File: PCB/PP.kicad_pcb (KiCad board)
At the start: 2 copper layers, 96.5 x 58.4 mm, 39 parts, among them Q1 Q_PMOS_DGS, Q2 Q_NMOS_DGS, Q3 Q_PMOS_DGS, Q4 Q_NMOS_DGS, U1 ESP32_DEVKITV1

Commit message: Update pouleporte releaseV2
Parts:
- removed 5V_batt1, AT1, AT2, CT1, CT2, GNDT1, GNDT2, GND_BAT1, backup_out1, backup_out2, capteurNCbas1, capteurNChaut1, capteur_NC3.3Vbas1, capteur_NC3.3Vhaut1, remote_AT1, remote_AT2, remote_CT1, remote_CT2, remote_gnd1, remote_gnd2: Conn_01x01, Connector_Pin:Pin_D1.2mm_L11.3mm_W3.0mm_Flat
- removed R3: 33, Resistor_SMD:R_0603_1608Metric
- removed R4: 10k, Resistor_SMD:R_0603_1608Metric
- removed R5, R6, R7: 12, Resistor_SMD:R_0603_1608Metric_Pad1.05x0.95mm_HandSolder
- removed capteurbas1, capteurhaut1: TCRT5000, wemos:TCRT5000
- added C1: 0.01uF, Capacitor_SMD:C_0603_1608Metric, F.Cu at (126.0, 77.0)
- added C2: 2.2uf, Capacitor_SMD:C_0603_1608Metric, F.Cu at (140.4, 63.6)
- added C3: 4.7uF, Capacitor_SMD:C_0603_1608Metric, F.Cu at (134.3, 70.3)
- added C4: 1uF, Capacitor_SMD:C_0603_1608Metric, F.Cu at (140.4, 61.1)
- added IN1: Conn_01x01, Connector_Pin:Pin_D1.2mm_L11.3mm_W3.0mm_Flat, F.Cu at (145.0, 76.0)
- added IN2: Conn_01x01, Connector_Pin:Pin_D1.2mm_L11.3mm_W3.0mm_Flat, F.Cu at (145.0, 81.2)
- added J1: USB_B_Micro, Connector_USB:USB_Micro-B_Wuerth_629105150521, F.Cu at (129.0, 47.8)
- added RESET1: SW_Push_Open, Library:interrupteur, F.Cu at (109.8, 77.8)
- added SWIO1: SW_Push_Open, Library:interrupteur, F.Cu at (96.8, 77.8)
- added U2: DRV8833PWP, Package_SO:HTSSOP-16-1EP_4.4x5mm_P0.65mm_EP3.4x5mm_Mask2.46x2.31mm_ThermalVias, F.Cu at (138.6, 56.5)
- added U3: AP7361C-33E, Package_TO_SOT_SMD:SOT-223-3_TabPin2, F.Cu at (128.5, 64.9)
- Q1, Q3: value Q_PMOS_DGS -> AO4425; footprint Package_TO_SOT_SMD:SOT-23 -> Package_SO_AKL:SO-8_3.9x4.9mm_P1.27mm
- Q2, Q4: value Q_NMOS_DGS -> AO3406; footprint Package_TO_SOT_SMD:SOT-23 -> Package_TO_SOT_SMD_AKL:SOT-23
- R1: value 33 -> 10k; footprint Resistor_SMD:R_0603_1608Metric -> Capacitor_SMD:C_0603_1608Metric
- R2: footprint Resistor_SMD:R_0603_1608Metric -> Capacitor_SMD:C_0603_1608Metric
- U1: value ESP32_DEVKITV1 -> ESP32-WROOM-32; footprint wemos:devkt1_online -> RF_Module:ESP32-WROOM-32
- moved capteurlux1 106.9 mm to (147.0, 51.0)
- moved U1 56.0 mm to (108.9, 65.5)
- moved Q3 55.8 mm to (137.2, 76.2)
- moved 3V3_lux1 55.4 mm to (147.0, 55.0)
- moved GNDlux1 54.1 mm to (147.0, 46.0)
- moved R1 49.3 mm to (109.0, 80.0), turned to 90 degrees
- moved R2 49.2 mm to (107.0, 80.0), turned to 90 degrees
- moved Q2 42.9 mm to (142.2, 68.6)
- moved Q1 40.0 mm to (127.9, 72.4)
- moved MOT2 38.2 mm to (147.0, 63.0), turned to 0 degrees
- moved MOT1 38.2 mm to (147.0, 68.0), turned to 0 degrees
- moved Q4 34.4 mm to (121.6, 78.9)
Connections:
- Q1 pad 1: Net-(MOT1-Pad1) -> 5V
- Q1 pad 2: Net-(Q1-Pad2) -> 5V
- Q2 pad 1: Net-(MOT1-Pad1) -> Net-(backup_out1-Pad1)
- Q2 pad 2: Net-(Q1-Pad2) -> GND
- Q2 pad 3: GND -> Net-(MOT1-Pad1)
- Q3 pad 1: Net-(Q3-Pad1) -> 5V
- Q3 pad 2: Net-(Q3-Pad2) -> unconnected-(Q3-Pad2)
- Q3 pad 3: 5V -> unconnected-(Q3-Pad3)
- Q4 pad 1: Net-(Q3-Pad1) -> Net-(backup_out2-Pad1)
- Q4 pad 2: Net-(Q3-Pad2) -> GND
- Q4 pad 3: GND -> Net-(MOT2-Pad1)
- R1 pad 1: Net-(AT1-Pad1) -> VCC
- R2 pad 2: Net-(CT1-Pad1) -> Net-(R2-Pad2)
- U1 pad 1: Net-(U1-Pad1) -> GND
- U1 pad 10: Net-(U1-Pad10) -> unconnected-(U1-Pad10)
- U1 pad 11: Net-(U1-Pad11) -> unconnected-(U1-Pad11)
- U1 pad 12: Net-(U1-Pad12) -> unconnected-(U1-Pad12)
- U1 pad 13: Net-(U1-Pad13) -> unconnected-(U1-Pad13)
- U1 pad 14: GND -> unconnected-(U1-Pad14)
- U1 pad 15: 5V -> GND
- U1 pad 16: Net-(U1-Pad16) -> unconnected-(U1-Pad16)
- U1 pad 17: Net-(U1-Pad17) -> unconnected-(U1-Pad17)
- U1 pad 18: Net-(U1-Pad18) -> unconnected-(U1-Pad18)
- U1 pad 19: Net-(U1-Pad19) -> unconnected-(U1-Pad19)
- U1 pad 2: Net-(U1-Pad2) -> VCC
- U1 pad 20: Net-(Q1-Pad2) -> unconnected-(U1-Pad20)
- U1 pad 21: Net-(U1-Pad21) -> unconnected-(U1-Pad21)
- U1 pad 22: Net-(U1-Pad22) -> unconnected-(U1-Pad22)
- U1 pad 23: Net-(U1-Pad23) -> unconnected-(U1-Pad23)
- U1 pad 24: Net-(U1-Pad24) -> unconnected-(U1-Pad24)
- U1 pad 25: Net-(Q3-Pad2) -> Net-(R2-Pad2)
- U1 pad 26: Net-(U1-Pad26) -> unconnected-(U1-Pad26)
- U1 pad 29: Net-(U1-Pad29) -> unconnected-(U1-Pad29)
- U1 pad 3: Net-(U1-Pad3) -> Net-(R1-Pad2)
- U1 pad 30: VCC -> Net-(backup_out2-Pad1)
- U1 pad 4: Net-(U1-Pad4) -> Net-(capteurlux1-Pad1)
- U1 pad 5: Net-(U1-Pad5) -> unconnected-(U1-Pad5)
- U1 pad 6: Net-(R1-Pad2) -> unconnected-(U1-Pad6)
- U1 pad 7: Net-(R3-Pad2) -> unconnected-(U1-Pad7)
- U1 pad 8: Net-(U1-Pad8) -> unconnected-(U1-Pad8)
- U1 pad 9: Net-(U1-Pad9) -> unconnected-(U1-Pad9)
- capteurlux1 pad 1: Net-(U1-Pad2) -> Net-(capteurlux1-Pad1)
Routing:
- net Net-(Q1-Pad2): track 77.1 -> 0.00 mm, vias 1 -> 0
- net Net-(backup_out2-Pad1): track 0.00 -> 74.0 mm, vias 0 -> 5
- net Net-(backup_out1-Pad1): track 0.00 -> 73.0 mm, vias 0 -> 2
- net Net-(Q3-Pad2): track 53.1 -> 0.00 mm, vias 2 -> 0
- net Net-(capteurlux1-Pad1): track 0.00 -> 52.2 mm, vias 0 -> 4
- net GND: track 16.7 -> 65.7 mm, vias 2 -> 11
- net Net-(U1-Pad27): track 0.00 -> 46.1 mm
- net Net-(R3-Pad2): track 41.7 -> 0.00 mm, vias 2 -> 0
- net Net-(MOT2-Pad1): track 35.3 -> 76.7 mm, vias 1 -> 2
- net Net-(AT2-Pad1): track 41.2 -> 0.00 mm, vias 2 -> 0
- net VCC: track 138.4 -> 98.0 mm, vias 7 -> 9
- net Net-(Q3-Pad1): track 36.8 -> 0.00 mm, vias 2 -> 0
- net Net-(C1-Pad2): track 0.00 -> 30.7 mm
- net Net-(R2-Pad2): track 0.00 -> 29.0 mm, vias 0 -> 2
- net Net-(U1-Pad28): track 0.00 -> 23.9 mm, vias 0 -> 2
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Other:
- board size 96.5 x 58.4 mm -> 56 x 42 mm
- net class Default removed
- board text added: "Pouleporte V2 Designed by MBE"
- board text removed: "POULEPORTE V1!!! Designed by M.BESSON"

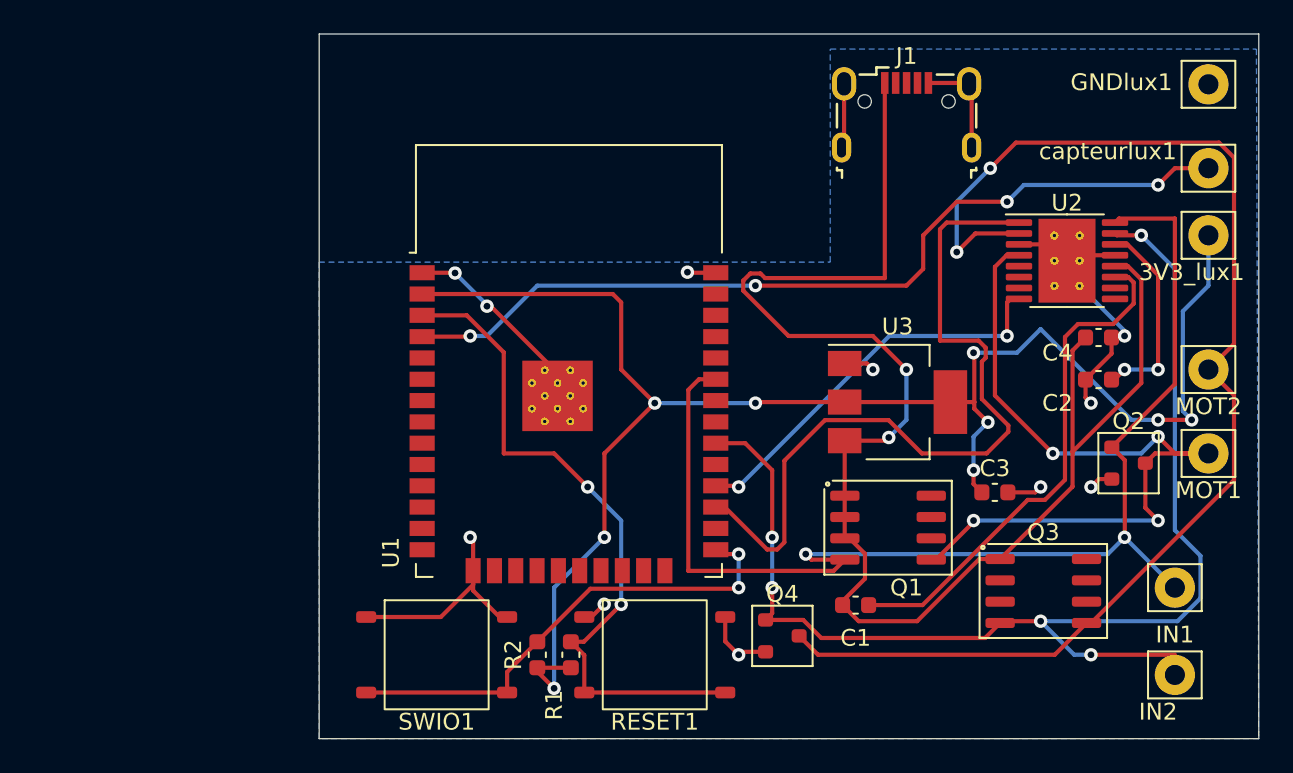
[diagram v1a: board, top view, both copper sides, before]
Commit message: adding usb and ap7361 libs
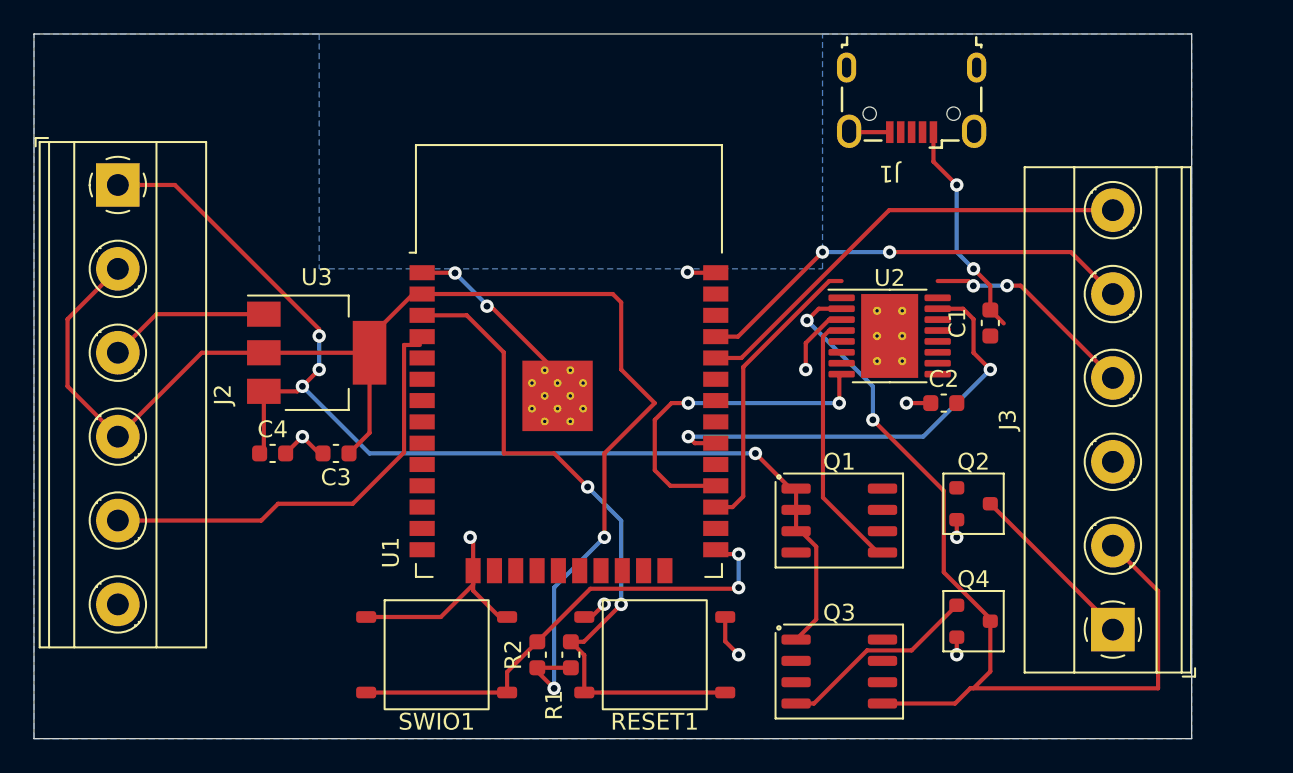
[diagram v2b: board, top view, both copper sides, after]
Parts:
- removed 3V3_lux1, GNDlux1, IN1, IN2, MOT1, MOT2, capteurlux1: Conn_01x01, Connector_Pin:Pin_D1.2mm_L11.3mm_W3.0mm_Flat
- added J2: Conn_01x06_Female, TerminalBlock_Phoenix:TerminalBlock_Phoenix_MKDS-1,5-6_1x06_P5.00mm_Horizontal, F.Cu at (82.0, 52.0)
- added J3: Conn_01x06_Female, TerminalBlock_Phoenix:TerminalBlock_Phoenix_MKDS-1,5-6_1x06_P5.00mm_Horizontal, F.Cu at (141.3, 78.5)
- J1: footprint Connector_USB:USB_Micro-B_Wuerth_629105150521 -> usb:USB_aliexpress
- U3: value AP7361C-33E -> AP7361ER
- moved C4 49.7 mm to (91.2, 68.0)
- moved C3 39.3 mm to (95.0, 68.0), turned to 180 degrees
- moved U3 34.7 mm to (93.8, 62.0)
- moved C1 18.6 mm to (134.0, 60.2), turned to -90 degrees
- moved Q3 13.1 mm to (125.0, 81.0)
- moved U2 11.5 mm to (128.0, 61.0)
- moved Q4 11.4 mm to (133.0, 78.0)
- moved Q2 9.55 mm to (133.0, 71.0)
- moved C2 9.33 mm to (131.2, 65.0)
- moved J1 3.17 mm to (128.0, 50.8), turned to 180 degrees
- moved Q1 2.94 mm to (125.0, 72.0)
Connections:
- U1 pad 34: unconnected-(U1-Pad34) -> Net-(U1-Pad34)
- U1 pad 35: unconnected-(U1-Pad35) -> Net-(U1-Pad35)
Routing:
- net Net-(Q1-Pad4): track 73.0 -> 12.8 mm
- net Net-(Q3-Pad4): track 74.0 -> 39.3 mm, vias 5 -> 2
- net Net-(C1-Pad2): track 30.7 -> 0.00 mm
- net Net-(U1-Pad27): track 46.1 -> 17.6 mm
- net Net-(U1-Pad34): track 0.00 -> 27.3 mm
- net Net-(U1-Pad35): track 0.00 -> 26.8 mm, vias 0 -> 2
- net Net-(U1-Pad4): track 52.2 -> 26.1 mm, vias 4 -> 0
- net Net-(Q3-Pad5): track 76.7 -> 55.6 mm
- net Net-(Q1-Pad5): track 46.6 -> 26.3 mm, vias 4 -> 0
- net VCC: track 98.0 -> 83.0 mm, vias 9 -> 2
- net GND: track 65.7 -> 52.0 mm
- net Net-(C2-Pad2): track 12.0 -> 0.00 mm, vias 2 -> 0
- net 5V: track 91.3 -> 80.8 mm, vias 2 -> 6
- net Net-(U1-Pad28): track 23.9 -> 20.2 mm
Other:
- board size 56 x 42 mm -> 69 x 42 mm

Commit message: Update schematic & pcb v3
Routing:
- net Net-(Q1-Pad4): track 12.8 -> 58.5 mm, vias 2 -> 7
- net 5V: track 80.8 -> 109.9 mm, vias 6 -> 8
- net Net-(Q3-Pad4): track 39.3 -> 60.1 mm, vias 2 -> 3
- net Net-(C2-Pad2): track 0.00 -> 11.5 mm, vias 0 -> 2
- net Net-(Q1-Pad5): track 26.3 -> 37.5 mm, vias 0 -> 2
- net Net-(C1-Pad2): track 0.00 -> 6.46 mm, vias 0 -> 2
- net GND: track 52.0 -> 54.2 mm
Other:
- board size 69 x 42 mm -> 69.5 x 42 mm
- board text added: "5V"
- board text added: "GND"
- board text added: "LUX"
- board text added: "MOT"
- board text added: "O18"
- board text added: "O21"
- board text added: "Pouleporte V3 Designed by MBE"
- board text added: "RX0"
- board text added: "TX0"
- board text added: "VCC"
- board text removed: "Pouleporte V2 Designed by MBE"
